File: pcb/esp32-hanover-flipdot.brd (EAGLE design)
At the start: 45.1 x 25.4 mm, 28 parts, among them J1 DC-005, J2 HANOVER, J3 FTDI, Q1 NCE3407A, Q2 S9013, U1 ESP32-PICO-D4, U2 CJA1117B-3.3-SOT89, U3 LM2576S

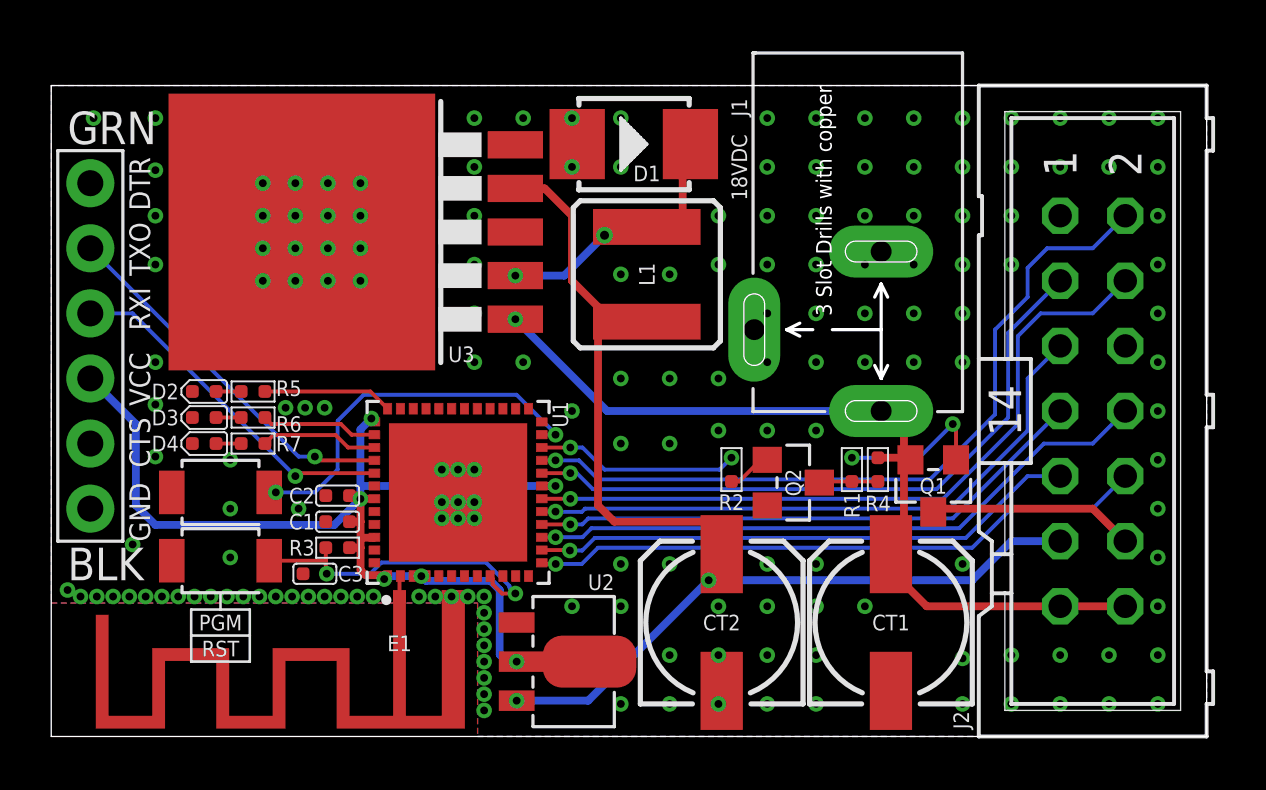
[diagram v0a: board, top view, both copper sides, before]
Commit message: PCB: Disconnect dot board pin 13, 14. Add 18VDC and warning text. Increase space around J2.
Disconnect dot-board pin 13 and 14 from 18VDC, seems to cause overheating of dot 0,0 on dot boards when boards are not enabled. Works fine without anyway - tested by cutting ribbon cable pins 13, 14.

Added 18VDC only warning text. Add warning text to disconnect power before connecting or disconnecting dot boards.

Increase space around J2 as the connector housing is causing stress to neighboring components.
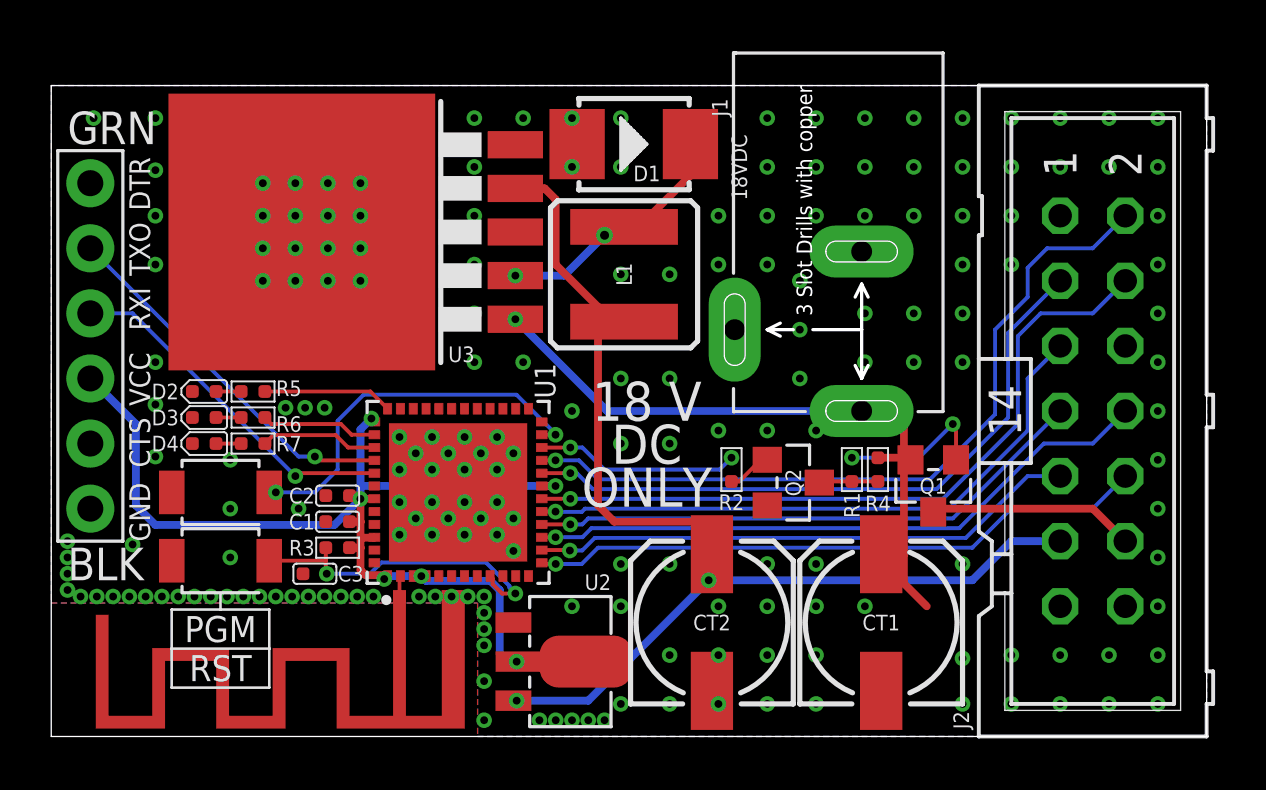
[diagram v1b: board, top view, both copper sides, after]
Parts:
- moved L1 0.89 mm to (22.4, 18.0)
- moved J1 0.76 mm to (31.6, 15.9)
- moved CT1 0.38 mm to (32.4, 4.45)
- moved CT2 0.38 mm to (25.8, 4.45)
- moved U2 0.13 mm to (19.9, 2.92)
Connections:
- net +18V: no longer J2.13, J2.14
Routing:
- net +18V: track 35.1 -> 27.7 mm
- net +5V: track 47.7 -> 46.3 mm
- net N$4: track 11.1 -> 9.95 mm
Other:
- board text added: "18 V DC ONLY"
- board text added: "WARNING: Always disconnect power supply before connecting or disconnecting dot boards!"

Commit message: Fix Eagle Seeedstudio DRC
Routed missing airwires and approved clearance issues
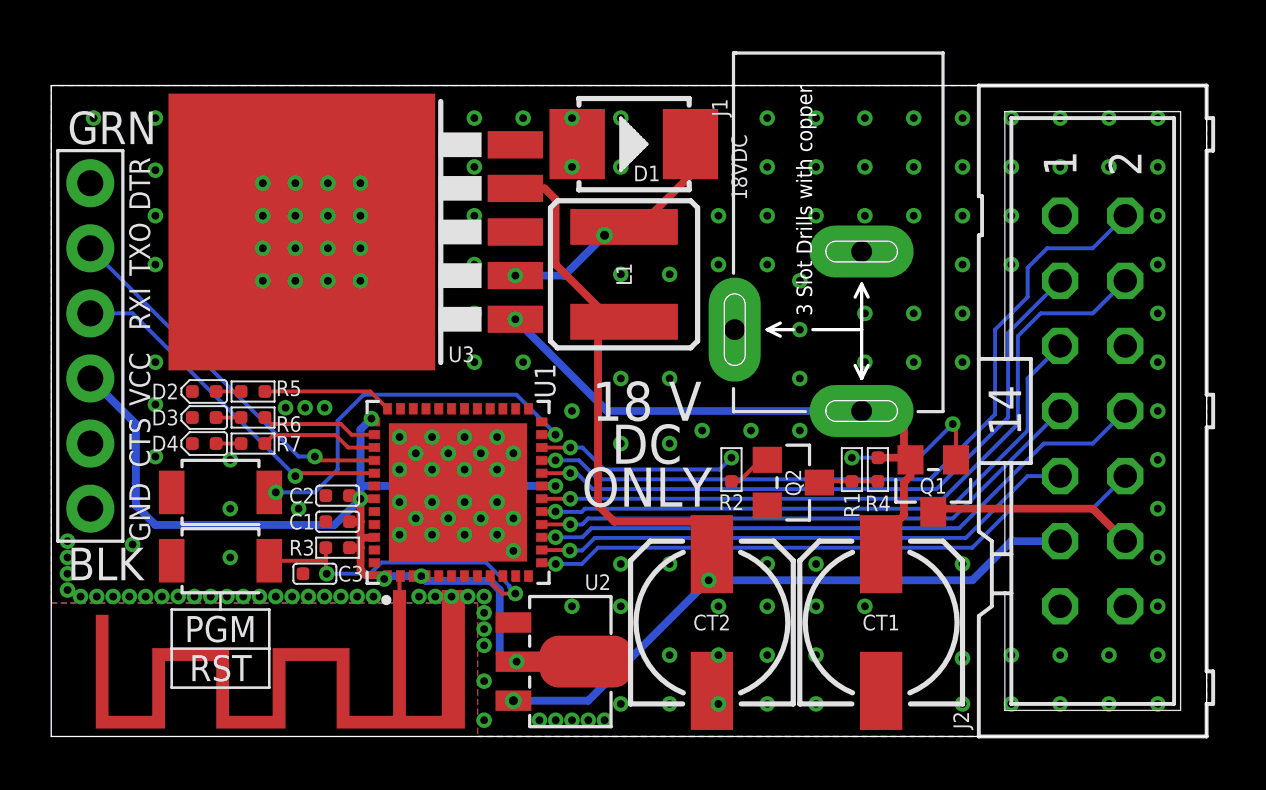
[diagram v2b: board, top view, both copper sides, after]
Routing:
- net +18V: track 27.7 -> 24.4 mm
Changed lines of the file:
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@@
 <element name="J1" library="Seeed-Connector" library_urn="urn:adsk.eagle:library:478" package="DCJ3P-14.2X11.0X9.0MM" package3d_urn="urn:adsk.eagle:package:33131/1" value="DC-005" x="31.623" y="15.875" smashed="yes" rot="R270">
 <attribute name="MPN" value="DC-005" x="31.623" y="15.875" size="1.778" layer="27" rot="R270" display="off"/>
+<attribute name="NAME" x="30.988" y="15.875" size="0.254" layer="33" ratio="10"/>
 <attribute name="NAME" x="25.781" y="24.892" size="0.6096" layer="25" ratio="11" rot="R270"/>
-<attribute name="NAME" x="30.988" y="15.875" size="0.254" layer="33" ratio="10"/>
 <attribute name="VALUE" x="30.988" y="25.4" size="0.889" layer="27" ratio="11" rot="R270"/>
 </element>
@@
 <element name="D1" library="Seeed-Diode" library_urn="urn:adsk.eagle:library:467" package="DO-214AA" package3d_urn="urn:adsk.eagle:package:32511/1" value="28V-5A" x="22.733" y="23.114" smashed="yes">
 <attribute name="MPN" value="SS54B" x="22.733" y="23.114" size="1.778" layer="27" display="off"/>
+<attribute name="NAME" x="24.003" y="23.114" size="0.5" layer="33" ratio="10" rot="R180"/>
 <attribute name="NAME" x="23.241" y="21.971" size="0.6096" layer="25" ratio="11" align="center"/>
-<attribute name="NAME" x="24.003" y="23.114" size="0.5" layer="33" ratio="10" rot="R180"/>
 <attribute name="VALUE" x="21.082" y="20.32" size="0.635" layer="27" ratio="10"/>
 </element>
@@
 <via x="29.845" y="6.731" extent="1-16" drill="0.3048"/>
 <via x="35.56" y="6.731" extent="1-16" drill="0.3048"/>
-<via x="29.845" y="11.938" extent="1-16" drill="0.3048"/>
-<via x="27.94" y="11.938" extent="1-16" drill="0.3048"/>
-<via x="26.035" y="11.938" extent="1-16" drill="0.3048"/>
+<via x="29.21" y="11.938" extent="1-16" drill="0.3048"/>
+<via x="27.305" y="11.938" extent="1-16" drill="0.3048"/>
+<via x="25.4" y="11.938" extent="1-16" drill="0.3048"/>
 <via x="16.129" y="10.414" extent="1-16" drill="0.3048"/>
 <via x="9.652" y="8.89" extent="1-16" drill="0.3048"/>
@@
 <contactref element="CT1" pad="+"/>
 <contactref element="U3" pad="1"/>
-<wire x1="32.385" y1="6.477" x2="32.385" y2="7.112" width="0.3048" layer="1"/>
 <via x="18.1102" y="16.2814" extent="1-16" drill="0.3048"/>
 <wire x1="21.6916" y1="12.7" x2="18.1102" y2="16.2814" width="0.3048" layer="16"/>
 <wire x1="31.623" y1="12.7" x2="21.6916" y2="12.7" width="0.3048" layer="16"/>
 <wire x1="31.623" y1="12.7" x2="33.274" y2="12.7" width="0.3048" layer="1"/>
-<wire x1="33.274" y1="7.112" x2="32.385" y2="7.112" width="0.3048" layer="1"/>
 <wire x1="33.274" y1="12.7" x2="33.274" y2="10.795" width="0.3048" layer="1"/>
-<wire x1="33.274" y1="10.795" x2="33.274" y2="7.112" width="0.3048" layer="1"/>
 <wire x1="33.528" y1="10.795" x2="33.274" y2="10.795" width="0.3048" layer="1"/>
-<wire x1="33.274" y1="5.969" x2="33.274" y2="7.112" width="0.3048" layer="1"/>
-<wire x1="34.163" y1="5.08" x2="33.274" y2="5.969" width="0.3048" layer="1"/>
 <wire x1="33.528" y1="10.795" x2="33.4465" y2="10.8765" width="0.3048" layer="1"/>
 <wire x1="33.4465" y1="10.8765" x2="32.258" y2="10.8765" width="0.3048" layer="1"/>
+<wire x1="33.528" y1="10.795" x2="33.528" y2="10.16" width="0.3048" layer="1"/>
+<wire x1="33.528" y1="10.16" x2="33.274" y2="9.906" width="0.3048" layer="1"/>
+<wire x1="33.274" y1="8.636" x2="33.274" y2="9.906" width="0.3048" layer="1"/>
+<wire x1="33.274" y1="8.636" x2="32.639" y2="8.001" width="0.3048" layer="1"/>
+<wire x1="32.385" y1="8.001" x2="32.639" y2="8.001" width="0.3048" layer="1"/>
+<wire x1="32.385" y1="7.112" x2="32.385" y2="8.001" width="0.3048" layer="1"/>
 </signal>
 <signal name="COIL_PULSE">
@@
 <contactref element="L1" pad="P$2"/>
 <via x="25.654" y="6.096" extent="1-16" drill="0.3048"/>
-<wire x1="25.654" y1="6.096" x2="20.955" y2="1.397" width="0.3048" layer="16"/>
-<wire x1="20.955" y1="1.397" x2="18.161" y2="1.397" width="0.3048" layer="16"/>
-<via x="18.161" y="1.397" extent="1-16" drill="0.3048"/>
+<wire x1="20.955" y1="1.397" x2="25.654" y2="6.096" width="0.3048" layer="16"/>
 <wire x1="35.941" y1="6.096" x2="25.654" y2="6.096" width="0.3048" layer="16"/>
 <wire x1="37.465" y1="7.62" x2="39.37" y2="7.62" width="0.3048" layer="16"/>
@@
 <wire x1="22.352" y1="16.184" x2="21.408" y2="16.184" width="0.3048" layer="1"/>
 <wire x1="21.408" y1="16.184" x2="21.336" y2="16.256" width="0.3048" layer="1"/>
-<wire x1="18.161" y1="1.397" x2="18.034" y2="1.397" width="0" layer="19" extent="1-1"/>
+<via x="18.034" y="1.397" extent="1-16" drill="0.35"/>
+<wire x1="18.034" y1="1.397" x2="20.955" y2="1.397" width="0.3048" layer="16"/>
 </signal>
 <signal name="N$1">
@@
 <contactref element="L1" pad="P$1"/>
 <via x="18.1102" y="17.9832" extent="1-16" drill="0.3048"/>
-<wire x1="22.352" y1="19.884" x2="22.225" y2="20.066" width="0.3048" layer="1"/>
 <via x="21.59" y="19.558" extent="1-16" drill="0.35"/>
 <wire x1="21.916" y1="19.884" x2="21.59" y2="19.558" width="0.3048" layer="1"/>
@@
 <wire x1="18.1102" y1="17.9832" x2="20.0152" y2="17.9832" width="0.3048" layer="16"/>
 <wire x1="21.59" y1="19.558" x2="20.0152" y2="17.9832" width="0.3048" layer="16"/>
-<wire x1="24.943" y1="23.114" x2="24.892" y2="23.114" width="0.3048" layer="1"/>
 <wire x1="24.943" y1="23.114" x2="24.943" y2="21.895" width="0.3048" layer="1"/>
 <wire x1="22.932" y1="19.884" x2="22.352" y2="19.884" width="0.3048" layer="1"/>
